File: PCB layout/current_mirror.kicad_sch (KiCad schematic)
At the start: 21 parts, among them J1 9.8V INPUT, Q1 2N3904, Q2 2N3904

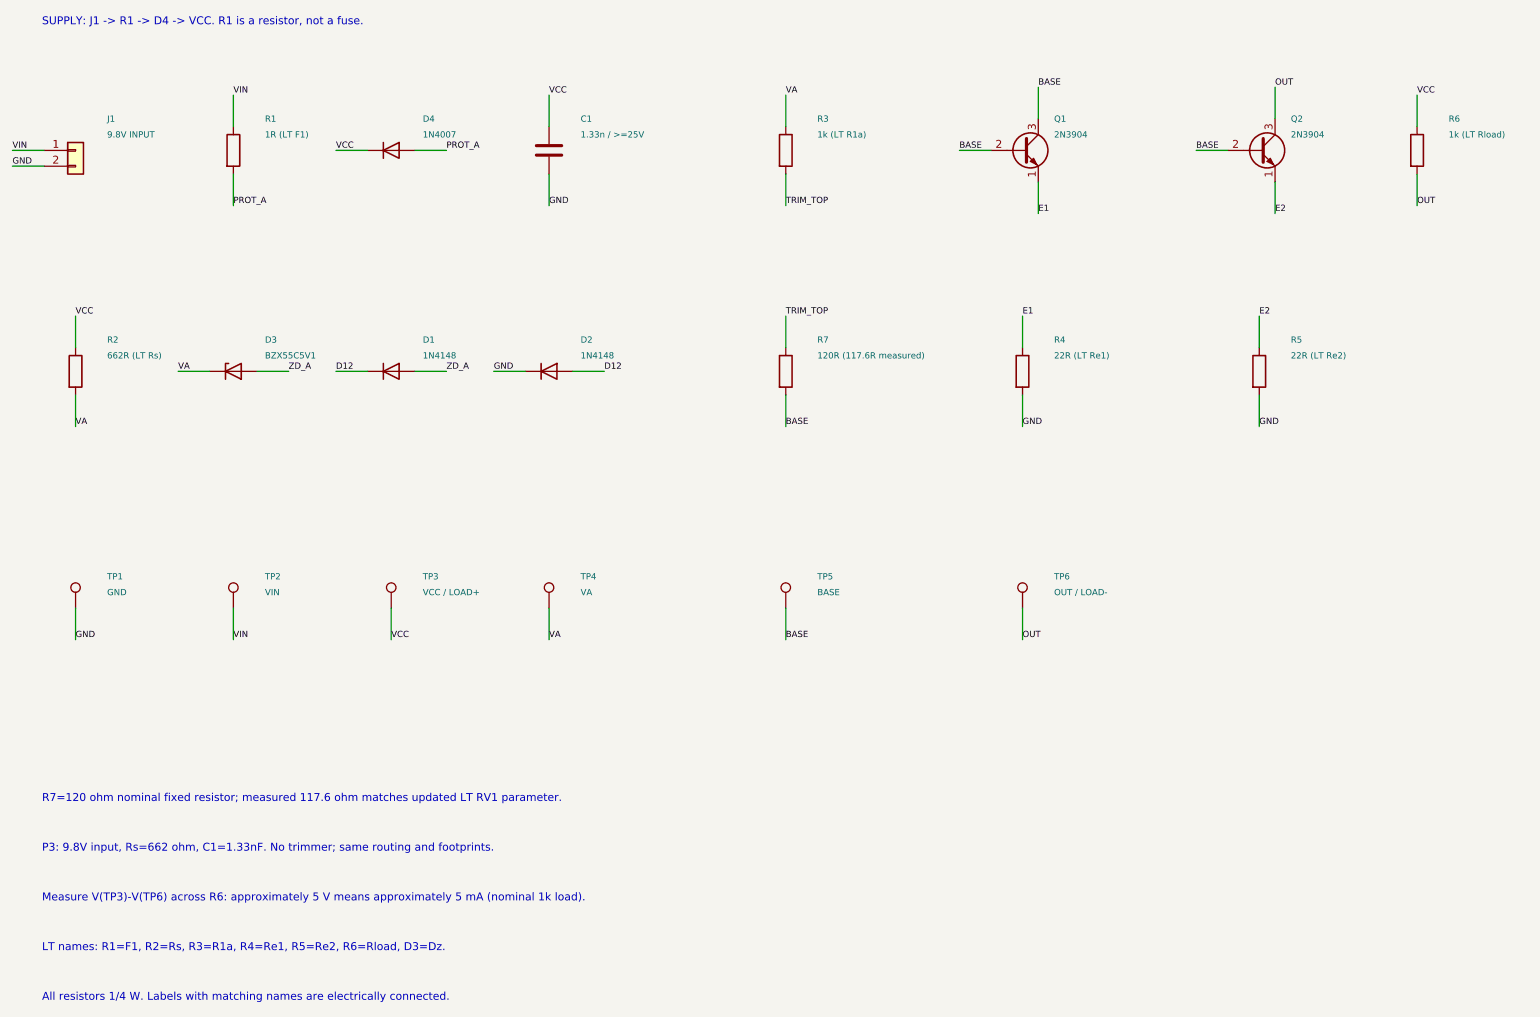
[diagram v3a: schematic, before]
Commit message: Add isolated dual current mirror panel with measurement headers
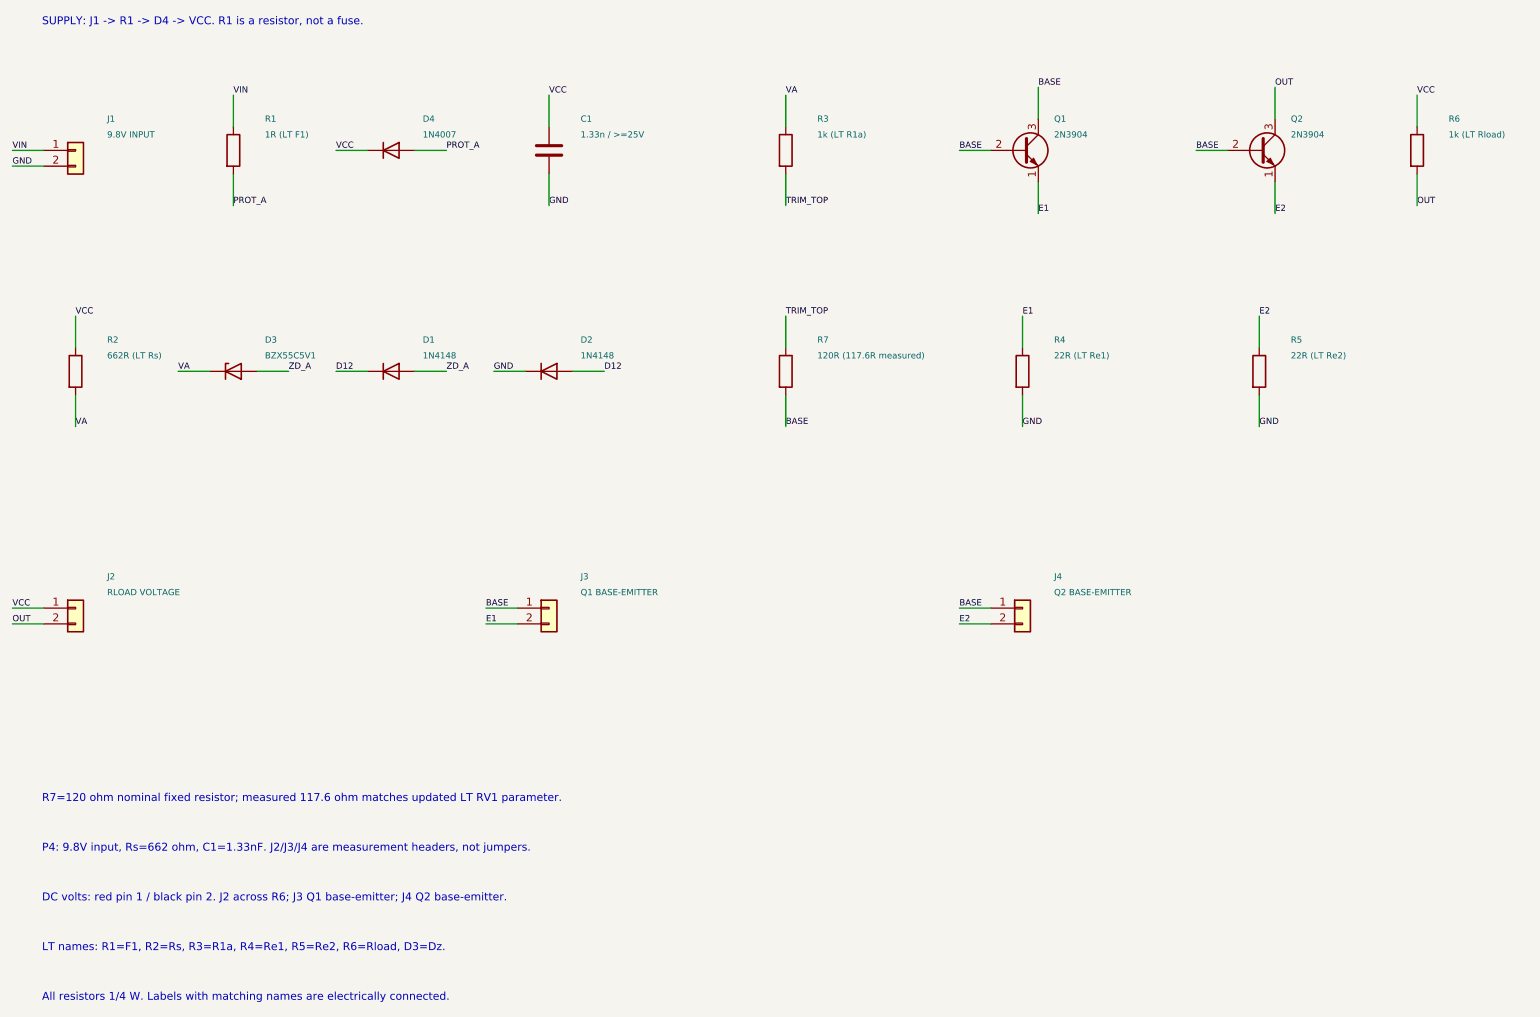
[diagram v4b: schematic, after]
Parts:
- removed TP1: GND, Project:TP1_ETCH, symbol Connector:TestPoint
- removed TP2: VIN, Project:TP2_ETCH, symbol Connector:TestPoint
- removed TP3: VCC / LOAD+, Project:TP3_ETCH, symbol Connector:TestPoint
- removed TP4: VA, Project:TP4_ETCH, symbol Connector:TestPoint
- removed TP5: BASE, Project:TP5_ETCH, symbol Connector:TestPoint
- removed TP6: OUT / LOAD-, Project:TP6_ETCH, symbol Connector:TestPoint
- added J2: RLOAD VOLTAGE, Project:J2_ETCH, symbol Connector_Generic:Conn_01x02
- added J3: Q1 BASE-EMITTER, Project:J3_ETCH, symbol Connector_Generic:Conn_01x02
- added J4: Q2 BASE-EMITTER, Project:J4_ETCH, symbol Connector_Generic:Conn_01x02
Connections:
- net BASE: now also J3.1 (Pin_1), J4.1 (Pin_1)
- net E1: now also J3.2 (Pin_2)
- net E2: now also J4.2 (Pin_2)
- net OUT: now also J2.2 (Pin_2)
- net VCC: now also J2.1 (Pin_1)
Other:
- note added: "DC volts: red pin 1 / black pin 2. J2 across R6; J3 Q1 base-emitter; J4 Q2 base-emitter."
- note added: "P4: 9.8V input, Rs=662 ohm, C1=1.33nF. J2/J3/J4 are measurement headers, not jumpers."
- note removed: "Measure V(TP3)-V(TP6) across R6: approximately 5 V means approximately 5 mA (nominal 1k load)."
- note removed: "P3: 9.8V input, Rs=662 ohm, C1=1.33nF. No trimmer; same routing and footprints."
- title: Diode-compensated current mirror -> Diode-compensated current mirror - header unit
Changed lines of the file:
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@@
 (kicad_sch (version 20250114) (generator "pcb_layout_script") (paper "A4")
-(title_block (title "Diode-compensated current mirror") (rev "P3 - SOURCE VALUES SYNC") (comment 1 "9.8V input; Rs=662R; C1=1.33nF; fixed R7=120R nominal, 117.6R measured"))
+(title_block (title "Diode-compensated current mirror - header unit") (rev "P4 - MEASUREMENT HEADERS") (comment 1 "J1 power; J2 load voltage; J3 Q1 Vbe; J4 Q2 Vbe. Pin 1 positive, pin 2 negative."))
 (symbol (lib_id "Connector_Generic:Conn_01x02") (at 25.4 40.64 0) (unit 1) (in_bom yes) (on_board yes) (dnp no)
 (property "Reference" "J1" (at 30.479999999999997 35.56 0) (effects (font (size 1.0 1.0)) (justify left) ))
@@
 (wire (pts (xy 241.3 44.45) (xy 241.3 49.53)) (stroke (width 0) (type default)))
 (label "OUT" (at 241.3 49.53 0) (effects (font (size 1.0 1.0)) (justify left bottom)))
-(symbol (lib_id "Connector:TestPoint") (at 25.4 114.3 0) (unit 1) (in_bom yes) (on_board yes) (dnp no)
-(property "Reference" "TP1" (at 30.479999999999997 109.22 0) (effects (font (size 1.0 1.0)) (justify left) ))
-(property "Value" "GND" (at 30.479999999999997 111.75999999999999 0) (effects (font (size 1.0 1.0)) (justify left) ))
-(property "Footprint" "Project:TP1_ETCH" (at 25.4 114.3 0) (effects (font (size 1.0 1.0)) (justify left) (hide yes)))
-(pin "1")
-(instances (project "current_mirror" (path "/9e16e4a6-c072-58dd-bcd3-75d7d6cad8fa" (reference "TP1") (unit 1)))))
-(wire (pts (xy 25.4 114.3) (xy 25.4 119.38)) (stroke (width 0) (type default)))
-(label "GND" (at 25.4 119.38 0) (effects (font (size 1.0 1.0)) (justify left bottom)))
-(symbol (lib_id "Connector:TestPoint") (at 50.8 114.3 0) (unit 1) (in_bom yes) (on_board yes) (dnp no)
-(property "Reference" "TP2" (at 55.879999999999995 109.22 0) (effects (font (size 1.0 1.0)) (justify left) ))
-(property "Value" "VIN" (at 55.879999999999995 111.75999999999999 0) (effects (font (size 1.0 1.0)) (justify left) ))
-(property "Footprint" "Project:TP2_ETCH" (at 50.8 114.3 0) (effects (font (size 1.0 1.0)) (justify left) (hide yes)))
-(pin "1")
-(instances (project "current_mirror" (path "/9e16e4a6-c072-58dd-bcd3-75d7d6cad8fa" (reference "TP2") (unit 1)))))
-(wire (pts (xy 50.8 114.3) (xy 50.8 119.38)) (stroke (width 0) (type default)))
-(label "VIN" (at 50.8 119.38 0) (effects (font (size 1.0 1.0)) (justify left bottom)))
-(symbol (lib_id "Connector:TestPoint") (at 76.2 114.3 0) (unit 1) (in_bom yes) (on_board yes) (dnp no)
-(property "Reference" "TP3" (at 81.28 109.22 0) (effects (font (size 1.0 1.0)) (justify left) ))
-(property "Value" "VCC / LOAD+" (at 81.28 111.75999999999999 0) (effects (font (size 1.0 1.0)) (justify left) ))
-(property "Footprint" "Project:TP3_ETCH" (at 76.2 114.3 0) (effects (font (size 1.0 1.0)) (justify left) (hide yes)))
-(pin "1")
-(instances (project "current_mirror" (path "/9e16e4a6-c072-58dd-bcd3-75d7d6cad8fa" (reference "TP3") (unit 1)))))
-(wire (pts (xy 76.2 114.3) (xy 76.2 119.38)) (stroke (width 0) (type default)))
-(label "VCC" (at 76.2 119.38 0) (effects (font (size 1.0 1.0)) (justify left bottom)))
-(symbol (lib_id "Connector:TestPoint") (at 101.6 114.3 0) (unit 1) (in_bom yes) (on_board yes) (dnp no)
-(property "Reference" "TP4" (at 106.67999999999999 109.22 0) (effects (font (size 1.0 1.0)) (justify left) ))
-(property "Value" "VA" (at 106.67999999999999 111.75999999999999 0) (effects (font (size 1.0 1.0)) (justify left) ))
-(property "Footprint" "Project:TP4_ETCH" (at 101.6 114.3 0) (effects (font (size 1.0 1.0)) (justify left) (hide yes)))
-(pin "1")
-(instances (project "current_mirror" (path "/9e16e4a6-c072-58dd-bcd3-75d7d6cad8fa" (reference "TP4") (unit 1)))))
-(wire (pts (xy 101.6 114.3) (xy 101.6 119.38)) (stroke (width 0) (type default)))
-(label "VA" (at 101.6 119.38 0) (effects (font (size 1.0 1.0)) (justify left bottom)))
-(symbol (lib_id "Connector:TestPoint") (at 139.7 114.3 0) (unit 1) (in_bom yes) (on_board yes) (dnp no)
-(property "Reference" "TP5" (at 144.78 109.22 0) (effects (font (size 1.0 1.0)) (justify left) ))
-(property "Value" "BASE" (at 144.78 111.75999999999999 0) (effects (font (size 1.0 1.0)) (justify left) ))
-(property "Footprint" "Project:TP5_ETCH" (at 139.7 114.3 0) (effects (font (size 1.0 1.0)) (justify left) (hide yes)))
-(pin "1")
-(instances (project "current_mirror" (path "/9e16e4a6-c072-58dd-bcd3-75d7d6cad8fa" (reference "TP5") (unit 1)))))
-(wire (pts (xy 139.7 114.3) (xy 139.7 119.38)) (stroke (width 0) (type default)))
-(label "BASE" (at 139.7 119.38 0) (effects (font (size 1.0 1.0)) (justify left bottom)))
-(symbol (lib_id "Connector:TestPoint") (at 177.8 114.3 0) (unit 1) (in_bom yes) (on_board yes) (dnp no)
-(property "Reference" "TP6" (at 182.88000000000002 109.22 0) (effects (font (size 1.0 1.0)) (justify left) ))
-(property "Value" "OUT / LOAD-" (at 182.88000000000002 111.75999999999999 0) (effects (font (size 1.0 1.0)) (justify left) ))
-(property "Footprint" "Project:TP6_ETCH" (at 177.8 114.3 0) (effects (font (size 1.0 1.0)) (justify left) (hide yes)))
-(pin "1")
-(instances (project "current_mirror" (path "/9e16e4a6-c072-58dd-bcd3-75d7d6cad8fa" (reference "TP6") (unit 1)))))
-(wire (pts (xy 177.8 114.3) (xy 177.8 119.38)) (stroke (width 0) (type default)))
-(label "OUT" (at 177.8 119.38 0) (effects (font (size 1.0 1.0)) (justify left bottom)))
+(symbol (lib_id "Connector_Generic:Conn_01x02") (at 25.4 114.3 0) (unit 1) (in_bom yes) (on_board yes) (dnp no)
+(property "Reference" "J2" (at 30.479999999999997 109.22 0) (effects (font (size 1.0 1.0)) (justify left) ))
+(property "Value" "RLOAD VOLTAGE" (at 30.479999999999997 111.75999999999999 0) (effects (font (size 1.0 1.0)) (justify left) ))
+(property "Footprint" "Project:J2_ETCH" (at 25.4 114.3 0) (effects (font (size 1.0 1.0)) (justify left) (hide yes)))
+(pin "1")
+(pin "2")
+(instances (project "current_mirror" (path "/9e16e4a6-c072-58dd-bcd3-75d7d6cad8fa" (reference "J2") (unit 1)))))
+(wire (pts (xy 20.32 114.3) (xy 15.24 114.3)) (stroke (width 0) (type default)))
+(label "VCC" (at 15.24 114.3 0) (effects (font (size 1.0 1.0)) (justify left bottom)))
+(wire (pts (xy 20.32 116.84) (xy 15.24 116.84)) (stroke (width 0) (type default)))
+(label "OUT" (at 15.24 116.84 0) (effects (font (size 1.0 1.0)) (justify left bottom)))
+(symbol (lib_id "Connector_Generic:Conn_01x02") (at 101.6 114.3 0) (unit 1) (in_bom yes) (on_board yes) (dnp no)
+(property "Reference" "J3" (at 106.67999999999999 109.22 0) (effects (font (size 1.0 1.0)) (justify left) ))
+(property "Value" "Q1 BASE-EMITTER" (at 106.67999999999999 111.75999999999999 0) (effects (font (size 1.0 1.0)) (justify left) ))
+(property "Footprint" "Project:J3_ETCH" (at 101.6 114.3 0) (effects (font (size 1.0 1.0)) (justify left) (hide yes)))
+(pin "1")
+(pin "2")
+(instances (project "current_mirror" (path "/9e16e4a6-c072-58dd-bcd3-75d7d6cad8fa" (reference "J3") (unit 1)))))
+(wire (pts (xy 96.52 114.3) (xy 91.44 114.3)) (stroke (width 0) (type default)))
+(label "BASE" (at 91.44 114.3 0) (effects (font (size 1.0 1.0)) (justify left bottom)))
+(wire (pts (xy 96.52 116.84) (xy 91.44 116.84)) (stroke (width 0) (type default)))
+(label "E1" (at 91.44 116.84 0) (effects (font (size 1.0 1.0)) (justify left bottom)))
+(symbol (lib_id "Connector_Generic:Conn_01x02") (at 177.8 114.3 0) (unit 1) (in_bom yes) (on_board yes) (dnp no)
+(property "Reference" "J4" (at 182.88000000000002 109.22 0) (effects (font (size 1.0 1.0)) (justify left) ))
+(property "Value" "Q2 BASE-EMITTER" (at 182.88000000000002 111.75999999999999 0) (effects (font (size 1.0 1.0)) (justify left) ))
+(property "Footprint" "Project:J4_ETCH" (at 177.8 114.3 0) (effects (font (size 1.0 1.0)) (justify left) (hide yes)))
+(pin "1")
+(pin "2")
+(instances (project "current_mirror" (path "/9e16e4a6-c072-58dd-bcd3-75d7d6cad8fa" (reference "J4") (unit 1)))))
+(wire (pts (xy 172.72 114.3) (xy 167.64 114.3)) (stroke (width 0) (type default)))
+(label "BASE" (at 167.64 114.3 0) (effects (font (size 1.0 1.0)) (justify left bottom)))
+(wire (pts (xy 172.72 116.84) (xy 167.64 116.84)) (stroke (width 0) (type default)))
+(label "E2" (at 167.64 116.84 0) (effects (font (size 1.0 1.0)) (justify left bottom)))
 (text "SUPPLY: J1 -> R1 -> D4 -> VCC. R1 is a resistor, not a fuse." (at 20 20 0) (effects (font (size 1.27 1.27)) (justify left)))
 (text "R7=120 ohm nominal fixed resistor; measured 117.6 ohm matches updated LT RV1 parameter." (at 20 145 0) (effects (font (size 1.27 1.27)) (justify left)))
-(text "P3: 9.8V input, Rs=662 ohm, C1=1.33nF. No trimmer; same routing and footprints." (at 20 153 0) (effects (font (size 1.27 1.27)) (justify left)))
-(text "Measure V(TP3)-V(TP6) across R6: approximately 5 V means approximately 5 mA (nominal 1k load)." (at 20 161 0) (effects (font (size 1.27 1.27)) (justify left)))
+(text "P4: 9.8V input, Rs=662 ohm, C1=1.33nF. J2/J3/J4 are measurement headers, not jumpers." (at 20 153 0) (effects (font (size 1.27 1.27)) (justify left)))
+(text "DC volts: red pin 1 / black pin 2. J2 across R6; J3 Q1 base-emitter; J4 Q2 base-emitter." (at 20 161 0) (effects (font (size 1.27 1.27)) (justify left)))
 (text "LT names: R1=F1, R2=Rs, R3=R1a, R4=Re1, R5=Re2, R6=Rload, D3=Dz." (at 20 169 0) (effects (font (size 1.27 1.27)) (justify left)))
 (text "All resistors 1/4 W. Labels with matching names are electrically connected." (at 20 177 0) (effects (font (size 1.27 1.27)) (justify left)))
